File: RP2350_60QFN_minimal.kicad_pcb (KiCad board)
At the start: 2 copper layers, 52 x 51 mm, 43 parts, among them J1 USB_B_Micro, J2 Conn_02x18_Odd_Even, J3 Conn_02x18_Odd_Even, J4 SM03B-SRSS-TB, SW1 SW_Push, SW2 SW_Push, U1 RP2350_60QFN, U2 NCP1117-3.3_SOT223, U3 W25Q128JVS, Y1 ABM8-272-T3

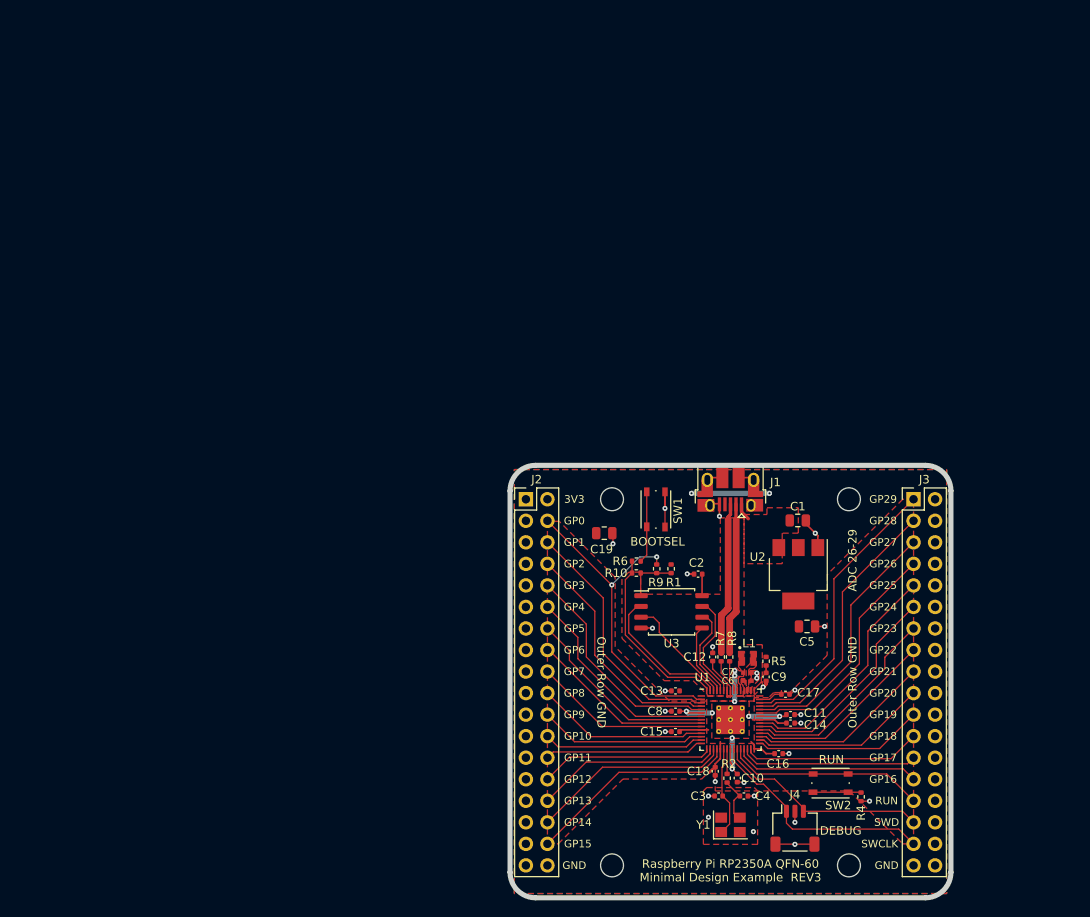
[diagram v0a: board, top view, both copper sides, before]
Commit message: Decent core PCB setup, considering removing USB to make space for flash
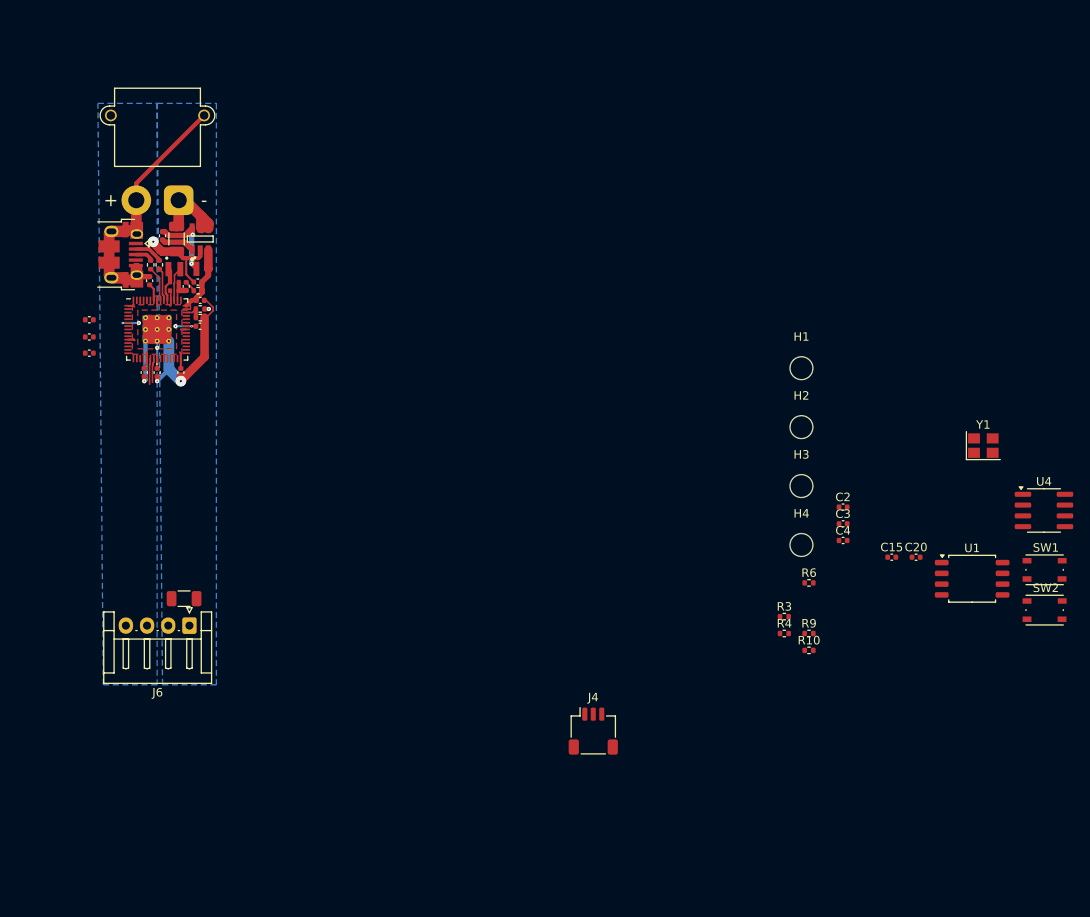
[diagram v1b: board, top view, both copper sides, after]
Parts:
- removed J3: Conn_02x18_Odd_Even, Connector_PinHeader_2.54mm:PinHeader_2x18_P2.54mm_Vertical
- added C20: 10u, Capacitor_SMD:C_0402_1005Metric, F.Cu at (121.9, 80.8)
- added C21: 100n, Capacitor_SMD:C_1206_3216Metric, F.Cu at (35.6, 85.7)
- added J6: Bus Out, Connector_JST:JST_EH_S4B-EH_1x04_P2.50mm_Horizontal, F.Cu at (36.2, 88.9)
- added L2: 3u3, RP2350_60QFN_minimal:L_pol_2016, F.Cu at (34.4, 46.9)
- added R3: 1K, Resistor_SMD:R_0402_1005Metric, F.Cu at (106.3, 87.8)
- added U4: MAX3078E, Package_SO:SOIC-8_3.9x4.9mm_P1.27mm, F.Cu at (137.0, 75.3)
- C1: value 10u -> 2u2; footprint Capacitor_SMD:C_0805_2012Metric -> Capacitor_SMD:C_1206_3216Metric
- C10, C7: value 4.7u -> 4u7
- C11: value 100n -> 4u7
- C19: value 10u -> 100n; footprint Capacitor_SMD:C_0805_2012Metric -> Capacitor_SMD:C_0402_1005Metric
- C2: value 100n -> 15p
- C4: value 15p -> 100n
- C5: value 10u -> 4u7; footprint Capacitor_SMD:C_0805_2012Metric -> RP2350_60QFN_minimal:C_0402_1005Metric_small_pads
- C6: value 4.7u -> 100n; footprint RP2350_60QFN_minimal:C_0402_1005Metric_small_pads -> Capacitor_SMD:C_0402_1005Metric
- C8: value 100n -> 10u
- C9: value 4.7u -> 100n
- J1: value USB_B_Micro -> Conn_01x02_Pin; footprint Connector_USB:USB_Micro-B_Amphenol_10103594-0001LF_Horizontal -> Connector_AMASS:AMASS_XT30PW-M_1x02_P2.50mm_Horizontal
- J2: value Conn_02x18_Odd_Even -> USB_B_Micro; footprint Connector_PinHeader_2.54mm:PinHeader_2x18_P2.54mm_Vertical -> Connector_USB:USB_Micro-B_Amphenol_10103594-0001LF_Horizontal
- R1, R9: value DNF -> 10K
- R10: value 0 -> 120R
- R2, R4, R6: value 1k -> 1K
- R5: value 33 -> 33R
- R7, R8: value 27 -> 27R
- U1: value RP2350_60QFN -> W25Q128JVS; footprint RP2350_60QFN_minimal:RP2350-QFN-60-1EP_7x7_P0.4mm_EP3.4x3.4mm_ThermalVias -> Package_SO:SOIC-8_5.3x5.3mm_P1.27mm
- U2: value NCP1117-3.3_SOT223 -> LMR50410Y3FQDBVRQ1; footprint Package_TO_SOT_SMD:SOT-223-3_TabPin2 -> footprints:DBV0006A-MFG
- U3: value W25Q128JVS -> RP2350_60QFN; footprint Package_SO:SOIC-8_5.23x5.23mm_P1.27mm -> RP2350_60QFN_minimal:RP2350-QFN-60-1EP_7x7_P0.4mm_EP3.4x3.4mm_ThermalVias
- moved C9 89.3 mm to (24.4, 54.9), turned to 180 degrees
- moved C18 88.8 mm to (24.4, 56.8), turned to 180 degrees
- moved C10 87.1 mm to (35.8, 48.9)
- moved C6 86.7 mm to (33.0, 42.9), turned to -90 degrees
- moved C14 85.6 mm to (37.5, 50.5)
- moved C11 84.9 mm to (32.4, 59.1), turned to -90 degrees
- moved C17 84.6 mm to (30.9, 59.1), turned to -90 degrees
- moved C5 84.5 mm to (34.4, 49.4)
- moved C16 83.6 mm to (35.2, 59.1), turned to -90 degrees
- moved R2 82.5 mm to (37.5, 52.6), turned to 0 degrees
- moved C7 81.8 mm to (34.4, 48.4)
- moved R7 81.6 mm to (31.6, 46.4)
- moved R8 81.6 mm to (32.6, 46.4)
- moved U2 80.9 mm to (37.5, 43.3), turned to 90 degrees
- moved C1 80.4 mm to (34.7, 43.3), turned to -90 degrees
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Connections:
- C1 pad 1: VBUS -> +24V
- C10 pad 1: +1V1 -> /VREG_AVDD
- C12 pad 1: +3V3 -> +1V1
- C2 pad 1: +3V3 -> /XIN
- C3 pad 1: /XIN -> Net-(C3-Pad1)
- C4 pad 1: Net-(C4-Pad1) -> +3V3
- C6 pad 1: +3V3 -> Net-(U2-SW)
- C6 pad 2: GND -> Net-(U2-CB)
- C8 pad 1: +1V1 -> +3V3
- C9 pad 1: /VREG_AVDD -> +1V1
- J1 pad 1: VBUS -> +24V
- J1 pad 2: /USB_D- -> GND
- J2 pad 1: GND -> unconnected-(J2-VBUS-Pad1)
- J2 pad 2: +3V3 -> /USB_D-
- J2 pad 3: GND -> /USB_D+
- J2 pad 4: /GPIO0 -> unconnected-(J2-ID-Pad4)
- J2 pad 6: /GPIO1 -> GND
- L1 pad 1: +1V1 -> Net-(U2-SW)
- L1 pad 2: /VREG_LX -> +3V3
- R1 pad 1: +3V3 -> +24V
- R1 pad 2: /FLASH_SS -> /GPIO29_ADC3
- R10 pad 1: /QSPI_SS -> /RS485-B
- R10 pad 2: /FLASH_SS -> /RS485-A
- R2 pad 1: /XOUT -> /GPIO29_ADC3
- R2 pad 2: Net-(C4-Pad1) -> GND
- R6 pad 1: /QSPI_SS -> /FLASH_SS
- R7 pad 2: Net-(U1-USB_DP) -> Net-(U3-USB_DP)
- R8 pad 2: Net-(U1-USB_DM) -> Net-(U3-USB_DM)
- R9 pad 1: /GPIO0 -> /GPIO7
- R9 pad 2: /FLASH_SS -> GND
- U1 pad 1: +3V3 -> /FLASH_SS
- U1 pad 2: /GPIO0 -> /QSPI_SD1
- U1 pad 3: /GPIO1 -> /QSPI_SD2
- U1 pad 4: /GPIO2 -> GND
- U1 pad 5: /GPIO3 -> /QSPI_SD0
- U1 pad 6: +1V1 -> /QSPI_SCLK
- U1 pad 7: /GPIO4 -> /QSPI_SD3
- U1 pad 8: /GPIO5 -> +3V3
- U2 pad 1: GND -> Net-(U2-CB)
- U2 pad 2: +3V3 -> GND
- U2 pad 3: VBUS -> +3V3
- U3 pad 1: /FLASH_SS -> +3V3
- U3 pad 2: /QSPI_SD1 -> /GPIO0
- U3 pad 3: /QSPI_SD2 -> /GPIO1
- U3 pad 4: GND -> /GPIO2
- U3 pad 5: /QSPI_SD0 -> /GPIO3
- U3 pad 6: /QSPI_SCLK -> +1V1
- U3 pad 7: /QSPI_SD3 -> /GPIO4
- U3 pad 8: +3V3 -> /GPIO5
- Y1 pad 3: Net-(C4-Pad1) -> Net-(C3-Pad1)
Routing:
- net /GPIO0: track 39.0 -> 0.00 mm, vias 2 -> 0
- net /GPIO28_ADC2: track 31.9 -> 0.00 mm
- net /GPIO29_ADC3: track 33.6 -> 2.32 mm
- net /GPIO27_ADC1: track 30.3 -> 0.00 mm
- net /GPIO1: track 29.8 -> 0.00 mm
- net GND: track 37.5 -> 67.0 mm, vias 27 -> 4
- net /GPIO26_ADC0: track 28.6 -> 0.00 mm
- net /GPIO2: track 28.2 -> 0.00 mm
- net /SWCLK: track 27.8 -> 0.00 mm
- net /GPIO25: track 27.7 -> 0.00 mm
- net /GPIO3: track 26.5 -> 0.00 mm
- net /GPIO24: track 26.1 -> 0.00 mm
- net /SWD: track 25.4 -> 0.00 mm
- net /GPIO15: track 25.2 -> 0.00 mm
- net /GPIO4: track 25.0 -> 0.00 mm
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- added copper zone on B.Cu, net +24V
- removed copper zone on F.Cu, net /VREG_LX
- removed copper zone on F.Cu, net GND
- removed copper zone on F.Cu, net VBUS
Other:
- board outline removed
- rule pad_to_mask_clearance: 0.051 -> 0
- board text removed: "3V3"
- board text removed: "ADC 26-29"
- board text removed: "BOOTSEL"
- board text removed: "DEBUG"
- board text removed: "GND"
- board text removed: "GP0"
- board text removed: "GP1"
- board text removed: "GP10"
- board text removed: "GP11"
- board text removed: "GP12"
- board text removed: "GP13"
- board text removed: "GP14"
- board text removed: "GP15"
- board text removed: "GP16"
- board text removed: "GP17"
- board text removed: "GP18"
- board text removed: "GP19"
- board text removed: "GP2"
- board text removed: "GP20"
- board text removed: "GP21"
- board text removed: "GP22"
- board text removed: "GP23"
- board text removed: "GP24"
- board text removed: "GP25"
- board text removed: "GP26"
- board text removed: "GP27"
- board text removed: "GP28"
- board text removed: "GP29"
- board text removed: "GP3"
- board text removed: "GP4"
- board text removed: "GP5"
- board text removed: "GP6"
- board text removed: "GP7"
- board text removed: "GP8"
- board text removed: "GP9"
- board text removed: "Minimal Design Example REV3"
- board text removed: "Outer Row GND"
- board text removed: "RUN"
- board text removed: "Raspberry Pi RP2350A QFN-60"
- board text removed: "SWCLK"
- board text removed: "SWD"

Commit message: fucking reversed polarity on the XT30
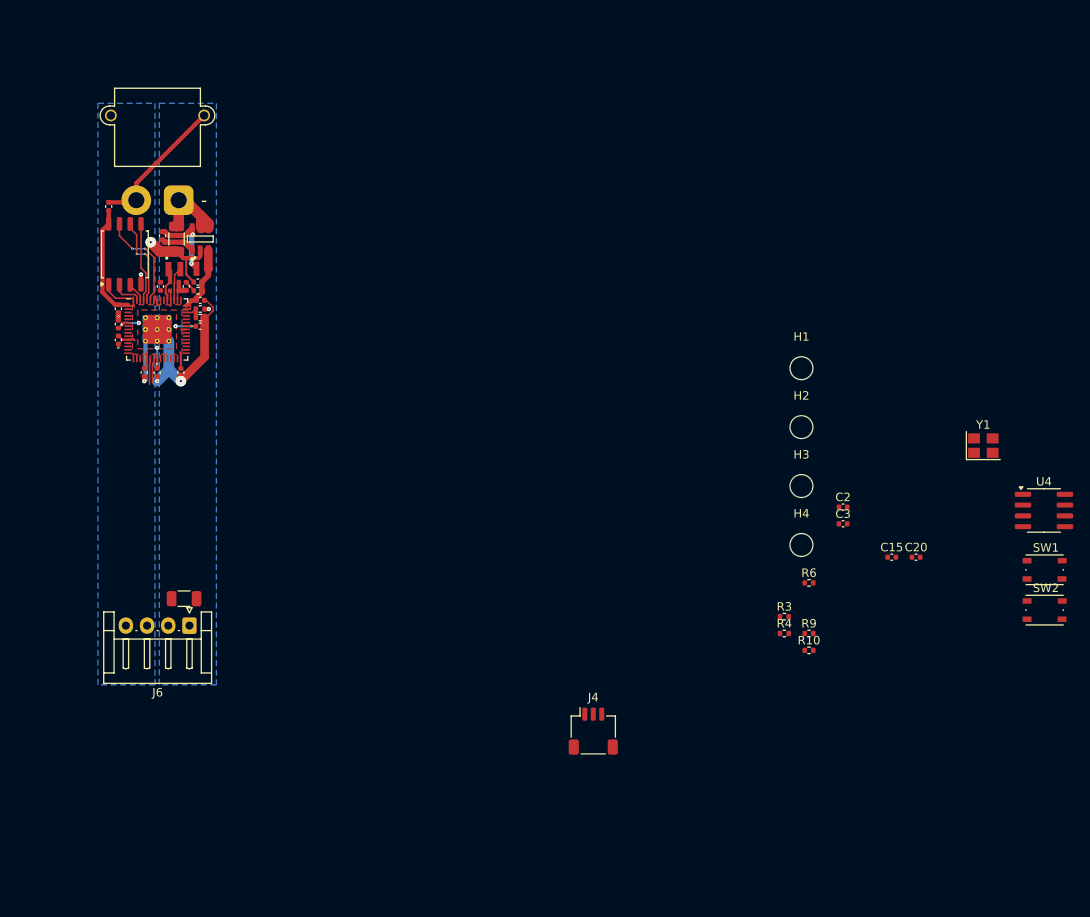
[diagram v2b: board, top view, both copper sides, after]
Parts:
- removed J2: USB_B_Micro, Connector_USB:USB_Micro-B_Amphenol_10103594-0001LF_Horizontal
- removed R7, R8: 27R, Resistor_SMD:R_0402_1005Metric
- moved U1 107.0 mm to (28.6, 45.1), turned to 90 degrees
- moved C4 95.1 mm to (26.7, 39.5), turned to 90 degrees
- moved C18 3.76 mm to (27.8, 55.2), turned to -90 degrees
- moved C9 3.75 mm to (27.8, 53.3), turned to 90 degrees
- moved C19 3.67 mm to (27.8, 51.5), turned to -90 degrees
- moved C13 1.43 mm to (32.8, 48.9)
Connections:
- J1 pad : GND -> (no net)
- J1 pad 1: +24V -> GND
- J1 pad 2: GND -> +24V
- U3 pad 51: Net-(U3-USB_DM) -> unconnected-(U3-USB_DM-Pad51)
- U3 pad 52: Net-(U3-USB_DP) -> unconnected-(U3-USB_DP-Pad52)
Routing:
- net +3V3: track 18.9 -> 31.7 mm
- net /QSPI_SD3: track 0.00 -> 11.8 mm, vias 0 -> 2
- net /QSPI_SCLK: track 0.00 -> 10.6 mm, vias 0 -> 2
- net /QSPI_SD0: track 0.00 -> 9.39 mm
- net GND: track 67.0 -> 58.0 mm, vias 4 -> 7
- net /FLASH_SS: track 0.00 -> 4.16 mm
- net Net-(U3-USB_DP): track 4.03 -> 0.00 mm
- net Net-(U3-USB_DM): track 3.90 -> 0.00 mm
- net /QSPI_SD1: track 0.00 -> 3.59 mm
- net /USB_D-: track 3.28 -> 0.00 mm
- net /QSPI_SD2: track 0.00 -> 2.35 mm
- net /USB_D+: track 2.17 -> 0.00 mm
- net +1V1: track 11.8 -> 13.5 mm

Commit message: Finished design without wifi & unchecked
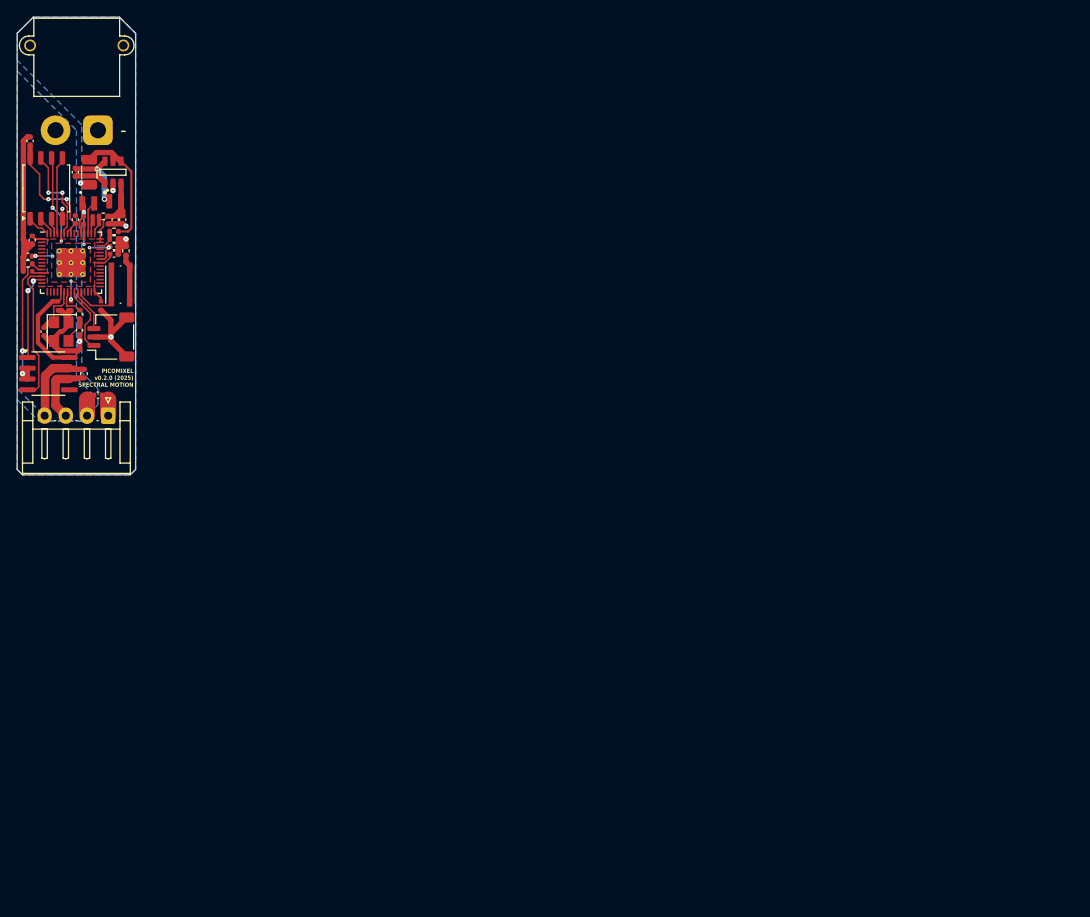
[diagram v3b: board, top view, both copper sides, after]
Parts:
- removed C21: 100n, Capacitor_SMD:C_1206_3216Metric
- removed H1, H2, H3, H4: MountingHole, MountingHole:MountingHole_2.7mm_M2.5
- removed J4: SM03B-SRSS-TB, Connector_JST:JST_SH_SM03B-SRSS-TB_1x03-1MP_P1.00mm_Horizontal
- removed J6: Bus Out, Connector_JST:JST_EH_S4B-EH_1x04_P2.50mm_Horizontal
- removed R10: 120R, Resistor_SMD:R_0402_1005Metric
- removed R9: 10K, Resistor_SMD:R_0402_1005Metric
- removed SW2: SW_Push, Button_Switch_SMD:SW_Push_1P1T_NO_Vertical_Wuerth_434133025816
- added J3: SM03B-SRSS-TB, Connector_JST:JST_SH_SM03B-SRSS-TB_1x03-1MP_P1.00mm_Horizontal, F.Cu at (26.9, 54.9)
- added J5: Bus Out, Connector_JST:JST_EH_S4B-EH_1x04_P2.50mm_Horizontal, F.Cu at (26.6, 64.1)
- added R7: 120R, Resistor_SMD:R_0402_1005Metric, F.Cu at (23.7, 59.2)
- C10, C11, C15, C17, C18: footprint Capacitor_SMD:C_0402_1005Metric -> RP2350_60QFN_minimal:C_0402_1005Metric_small_pads
- C20: value 10u -> 100n
- R6: value 1K -> 10K
- moved U4 118.5 mm to (19.6, 59.2)
- moved SW1 114.1 mm to (28.1, 48.7), turned to -90 degrees
- moved Y1 109.6 mm to (21.1, 54.2), turned to -90 degrees
- moved R6 99.5 mm to (17.1, 46.2), turned to 180 degrees
- moved C20 98.4 mm to (25.4, 61.7)
- moved C15 97.9 mm to (25.8, 51.2), turned to -90 degrees
- moved C2 96.5 mm to (19.1, 54.2), turned to -90 degrees
- moved C3 92.9 mm to (23.2, 54.1), turned to -90 degrees
- moved R3 90.4 mm to (23.2, 52.2), turned to -90 degrees
- moved R4 89.8 mm to (28.7, 44.7), turned to 90 degrees
- moved C16 23.5 mm to (17.7, 43.4)
- moved C12 21.9 mm to (17.1, 45.3), turned to 180 degrees
- moved C17 18.2 mm to (17.1, 47.1), turned to 180 degrees
- moved R5 14.2 mm to (26.0, 40.6)
- moved R2 13.8 mm to (27.3, 43.3)
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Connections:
- C20 pad 1: +3V3 -> +24V
- J1 pad : (no net) -> GND
- R6 pad 1: /FLASH_SS -> /GPIO7
- R6 pad 2: /~{USB_BOOT} -> GND
- SW1 pad 1: GND -> Net-(R4-Pad1)
- SW1 pad 2: /~{USB_BOOT} -> /RUN
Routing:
- net /GPIO7: track 0.00 -> 17.9 mm, vias 0 -> 2
- net +3V3: track 31.7 -> 49.1 mm, vias 0 -> 2
- net /GPIO8: track 0.00 -> 16.5 mm
- net /GPIO9: track 0.00 -> 10.4 mm, vias 0 -> 2
- net /RS485-B: track 0.00 -> 9.73 mm
- net /RUN: track 0.00 -> 8.87 mm
- net /RS485-A: track 0.00 -> 8.13 mm
- net /SWCLK: track 0.00 -> 8.00 mm
- net +24V: track 10.2 -> 17.6 mm, vias 1 -> 0
- net +1V1: track 13.5 -> 19.1 mm, vias 6 -> 8
- net Net-(R4-Pad1): track 0.00 -> 5.56 mm
- net /SWD: track 0.00 -> 5.11 mm
- net Net-(C3-Pad1): track 0.00 -> 3.16 mm
- net /XIN: track 3.07 -> 6.08 mm
- net GND: track 58.0 -> 60.2 mm
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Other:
- board outline added: 14 x 54 mm
- board text added: "PICOMIXEL"
- board text added: "PICOMIXEL v0.2.0 (2025) SPECTRAL MOTION"
- board text added: "POWER INPUT THROUGH TO DYNAMIXELS SAFE RANGE: 4V-36V XT30 CONNECTOR"
- board text added: "THE PEERLESS POWER PURVEYOR & PROGRAMMING PROTOCOL WITH PANACHE: THE"
- board text added: "WITH AN RP2350A CORE AND 16MB EXTERNAL FLASH MEMORY"

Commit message: Finished, checked design (still no WiFi)
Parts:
- moved C13 0.13 mm to (22.6, 41.0)
- moved C14 0.13 mm to (27.4, 45.1)
- moved C9 0.13 mm to (27.4, 44.2)
- moved R1 0.13 mm to (27.4, 42.4)
- moved R2 0.13 mm to (27.4, 43.3)
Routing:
- net GND: track 60.2 -> 80.4 mm, vias 7 -> 10
- net +3V3: track 49.1 -> 54.9 mm
- net +24V: track 17.6 -> 23.1 mm, vias 0 -> 1
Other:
- board text added: "DESIGNED AND PROGRAMMED BY WILL STURGEON AT SPECTRAL MOTION, INC."
- board text added: "RP2350A CORE + 16MB EXTERNAL FLASH MEMORY"
- board text removed: "WITH AN RP2350A CORE AND 16MB EXTERNAL FLASH MEMORY"
